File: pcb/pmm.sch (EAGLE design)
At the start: 20 parts, among them IC3 STM32F042F4, SW3 324_SW, SW4 324_SW, U2 USBC_16P, U4 XC6206_DEV

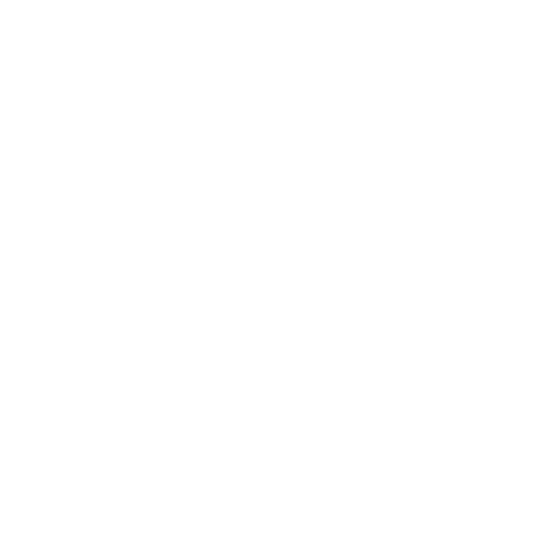
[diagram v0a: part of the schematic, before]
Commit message: hotshoe done
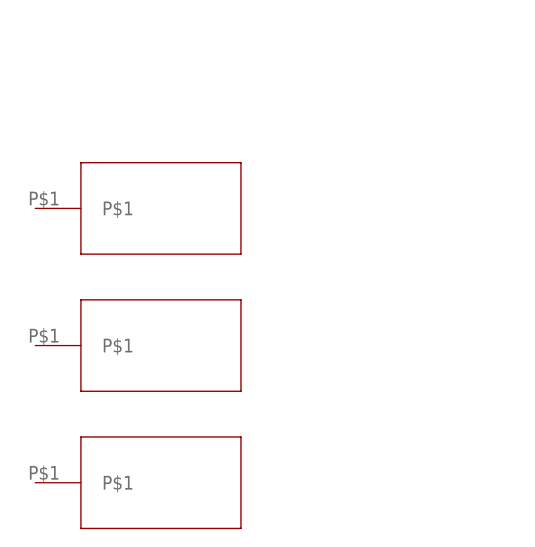
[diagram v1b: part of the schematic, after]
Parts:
- added U$3, U$4, U$5: POGO_1.5MM_HOLE, apricot:POGO_1.5MM_HOLE
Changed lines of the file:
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@@
 <layer number="117" name="secv21" color="7" fill="1" visible="yes" active="yes"/>
 <layer number="118" name="Rect_Pads" color="7" fill="1" visible="yes" active="yes"/>
+<layer number="119" name="PF_Ref" color="7" fill="1" visible="yes" active="yes"/>
 <layer number="120" name="120" color="7" fill="1" visible="yes" active="yes"/>
 <layer number="121" name="_tsilk" color="7" fill="1" visible="yes" active="yes"/>
@@
 <layer number="131" name="tAdjust" color="7" fill="1" visible="yes" active="yes"/>
 <layer number="132" name="bAdjust" color="7" fill="1" visible="yes" active="yes"/>
+<layer number="133" name="bottom_silk" color="7" fill="1" visible="yes" active="yes"/>
+<layer number="134" name="silk_top" color="7" fill="1" visible="yes" active="yes"/>
+<layer number="135" name="silk_bottom" color="7" fill="1" visible="yes" active="yes"/>
+<layer number="136" name="silktop" color="7" fill="1" visible="yes" active="yes"/>
+<layer number="137" name="silkbottom" color="7" fill="1" visible="yes" active="yes"/>
+<layer number="138" name="EEE" color="7" fill="1" visible="yes" active="yes"/>
+<layer number="139" name="_tKeepout" color="7" fill="1" visible="yes" active="yes"/>
+<layer number="140" name="mbKeepout" color="7" fill="1" visible="yes" active="yes"/>
+<layer number="141" name="ASSEMBLY_TOP" color="7" fill="1" visible="yes" active="yes"/>
+<layer number="142" name="mbRestrict" color="7" fill="1" visible="yes" active="yes"/>
+<layer number="143" name="PLACE_BOUND_TOP" color="7" fill="1" visible="yes" active="yes"/>
 <layer number="144" name="Drill_legend" color="7" fill="1" visible="yes" active="yes"/>
 <layer number="145" name="DrillLegend_01-02" color="7" fill="1" visible="yes" active="yes"/>
@@
 <layer number="154" name="FabDoc2" color="7" fill="1" visible="yes" active="yes"/>
 <layer number="155" name="FabDoc3" color="7" fill="1" visible="yes" active="yes"/>
+<layer number="166" name="AntennaArea" color="7" fill="1" visible="yes" active="yes"/>
+<layer number="168" name="4mmHeightArea" color="7" fill="1" visible="yes" active="yes"/>
+<layer number="191" name="mNets" color="7" fill="1" visible="yes" active="yes"/>
+<layer number="192" name="mBusses" color="7" fill="1" visible="yes" active="yes"/>
+<layer number="193" name="mPins" color="7" fill="1" visible="yes" active="yes"/>
+<layer number="194" name="mSymbols" color="7" fill="1" visible="yes" active="yes"/>
+<layer number="195" name="mNames" color="7" fill="1" visible="yes" active="yes"/>
+<layer number="196" name="mValues" color="7" fill="1" visible="yes" active="yes"/>
 <layer number="199" name="Contour" color="7" fill="1" visible="yes" active="yes"/>
 <layer number="200" name="200bmp" color="1" fill="10" visible="no" active="no"/>
@@
 <layer number="250" name="Descript" color="3" fill="1" visible="no" active="no"/>
 <layer number="251" name="SMDround" color="12" fill="11" visible="no" active="no"/>
+<layer number="253" name="Extra" color="7" fill="1" visible="yes" active="yes"/>
 <layer number="254" name="cooling" color="7" fill="1" visible="yes" active="yes"/>
 <layer number="255" name="routoute" color="7" fill="1" visible="yes" active="yes"/>
@@
 <part name="U$1" library="3pos_slide_switch_centered" deviceset="M2_SCREW_DEV" device=""/>
 <part name="U$2" library="3pos_slide_switch_centered" deviceset="M2_SCREW_DEV" device=""/>
+<part name="U$3" library="apricot" deviceset="POGO_1.5MM_HOLE" device=""/>
+<part name="U$4" library="apricot" deviceset="POGO_1.5MM_HOLE" device=""/>
+<part name="U$5" library="apricot" deviceset="POGO_1.5MM_HOLE" device=""/>
 </parts>
 <sheets>
@@
 <instance part="U$1" gate="G$1" x="-66.04" y="114.3" smashed="yes"/>
 <instance part="U$2" gate="G$1" x="-66.04" y="101.6" smashed="yes"/>
+<instance part="U$3" gate="G$1" x="-88.9" y="5.08" smashed="yes"/>
+<instance part="U$4" gate="G$1" x="-88.9" y="-10.16" smashed="yes"/>
+<instance part="U$5" gate="G$1" x="-88.9" y="-25.4" smashed="yes"/>
 </instances>
 <busses>

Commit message: working on PCB
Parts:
- added BT1: BU2032SM-G, BU2032SM-G:BU2032SM-G
- added C20, C21: 1uF, clock:CAP0805
- added C22, C23: 2.2uF, clock:CAP0805
- added J1: AUDIO_JACK_3.5MM_PTH, SparkFun-Connectors:AUDIO_JACK_3.5MM_PTH
- added J2: FFC3B07-05-T, FFC3B07-05-T:FFC3B07-05-T
- added R7: 390K, SparkFun-Passives:RESISTOR0805-RES
- added R8: 5.1K, joyAnalog:RESISTOR0805-RES
- added SW1: (no value), tx:SWITCH-SPDTTDFGDFG
- added U1: (no value), lul:LUL_DISP_OLED_UG-2864HSWEG01
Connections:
- new net N$12: U1.SDIN
- new net N$14: U1.SCLK
- new net N$16: U1.DC
- new net N$35: C20.2, U1.C2P
- new net N$36: C20.1, U1.C2N
- new net N$37: C21.2, U1.C1P
- new net N$38: C21.1, U1.C1N
- new net N$39: R7.2, U1.IREF
- new net N$40: C22.2, U1.VCOMH
- new net N$41: C23.2, U1.VCC
- new net N$43: R8.1, U1./RES
- net +3V3: now also U1.VBAT, U1.VDD
- net GND: now also C22.1, C23.1, R7.1, R8.2, U1.VSS
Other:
- moved on the sheet: C1, C2, R1, R2

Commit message: working on PCB
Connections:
- net N$16 renamed OLED_DC
- net N$3 renamed SWCLK
- net N$4 renamed SWDIO
- net N$43 renamed OLED_RESET
- net N$6 renamed UART2_TX
- removed net N$12: U1.SDIN
- removed net N$14: U1.SCLK
- new net OLED_CS: U1./CS
- new net OLED_MOSI: IC3.PA7, U1.SDIN
- new net OLED_SCK: IC3.PA5, U1.SCLK
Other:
- moved on the sheet: BT1, LED1, LED3, R3, R4
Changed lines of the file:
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@@
 <part name="R3" library="SparkFun-Passives" deviceset="RESISTOR" device="0805-RES" value="1K"/>
 <part name="+3V4" library="backplane" deviceset="+3V3" device=""/>
-<part name="+3V6" library="supply1" library_urn="urn:adsk.eagle:library:371" deviceset="+3V3" device=""/>
-<part name="GND3" library="backplane" deviceset="GND" device=""/>
 <part name="+3V3" library="supply1" library_urn="urn:adsk.eagle:library:371" deviceset="+3V3" device=""/>
 <part name="U$12" library="3pos_slide_switch_centered" deviceset="M2_SCREW_DEV" device=""/>
@@
 <instance part="SW3" gate="G$1" x="91.44" y="55.88" smashed="yes" rot="R90"/>
 <instance part="SW4" gate="G$1" x="91.44" y="2.54" smashed="yes" rot="MR270"/>
-<instance part="LED1" gate="G$1" x="-71.12" y="53.34" smashed="yes" rot="R90">
-<attribute name="NAME" x="-66.548" y="56.896" size="1.778" layer="95" rot="R180"/>
-<attribute name="VALUE" x="-66.548" y="59.055" size="1.778" layer="96" rot="R180"/>
-</instance>
-<instance part="R4" gate="G$1" x="-60.96" y="53.34" smashed="yes" rot="R180">
-<attribute name="NAME" x="-57.15" y="51.8414" size="1.778" layer="95" rot="R180"/>
-<attribute name="VALUE" x="-57.15" y="56.642" size="1.778" layer="96" rot="R180"/>
-</instance>
-<instance part="+3V9" gate="G$1" x="-73.66" y="55.88" smashed="yes" rot="MR0">
-<attribute name="VALUE" x="-71.12" y="50.8" size="1.778" layer="96" rot="MR90"/>
+<instance part="LED1" gate="G$1" x="-25.4" y="-45.72" smashed="yes" rot="R90">
+<attribute name="NAME" x="-20.828" y="-42.164" size="1.778" layer="95" rot="R180"/>
+<attribute name="VALUE" x="-20.828" y="-40.005" size="1.778" layer="96" rot="R180"/>
+</instance>
+<instance part="R4" gate="G$1" x="-15.24" y="-45.72" smashed="yes" rot="R180">
+<attribute name="NAME" x="-11.43" y="-47.2186" size="1.778" layer="95" rot="R180"/>
+<attribute name="VALUE" x="-11.43" y="-42.418" size="1.778" layer="96" rot="R180"/>
+</instance>
+<instance part="+3V9" gate="G$1" x="-27.94" y="-43.18" smashed="yes" rot="MR0">
+<attribute name="VALUE" x="-25.4" y="-48.26" size="1.778" layer="96" rot="MR90"/>
 </instance>
 <instance part="+3V16" gate="G$1" x="106.68" y="73.66" smashed="yes" rot="MR0">
@@
 <attribute name="VALUE" x="343.916" y="30.099" size="1.778" layer="96" rot="R180"/>
 </instance>
-<instance part="LED3" gate="G$1" x="-71.12" y="43.18" smashed="yes" rot="R90">
-<attribute name="NAME" x="-66.548" y="46.736" size="1.778" layer="95" rot="R180"/>
-<attribute name="VALUE" x="-66.548" y="48.895" size="1.778" layer="96" rot="R180"/>
-</instance>
-<instance part="R3" gate="G$1" x="-60.96" y="43.18" smashed="yes" rot="R180">
-<attribute name="NAME" x="-57.15" y="41.6814" size="1.778" layer="95" rot="R180"/>
-<attribute name="VALUE" x="-57.15" y="46.482" size="1.778" layer="96" rot="R180"/>
-</instance>
-<instance part="+3V4" gate="G$1" x="-73.66" y="45.72" smashed="yes" rot="MR0">
-<attribute name="VALUE" x="-71.12" y="40.64" size="1.778" layer="96" rot="MR90"/>
-</instance>
-<instance part="+3V6" gate="G$1" x="-27.94" y="66.04" smashed="yes" rot="MR0">
-<attribute name="VALUE" x="-25.4" y="60.96" size="1.778" layer="96" rot="MR90"/>
-</instance>
-<instance part="GND3" gate="1" x="-17.78" y="55.88" smashed="yes">
-<attribute name="VALUE" x="-20.32" y="53.34" size="1.778" layer="96"/>
+<instance part="LED3" gate="G$1" x="-25.4" y="-55.88" smashed="yes" rot="R90">
+<attribute name="NAME" x="-20.828" y="-52.324" size="1.778" layer="95" rot="R180"/>
+<attribute name="VALUE" x="-20.828" y="-50.165" size="1.778" layer="96" rot="R180"/>
+</instance>
+<instance part="R3" gate="G$1" x="-15.24" y="-55.88" smashed="yes" rot="R180">
+<attribute name="NAME" x="-11.43" y="-57.3786" size="1.778" layer="95" rot="R180"/>
+<attribute name="VALUE" x="-11.43" y="-52.578" size="1.778" layer="96" rot="R180"/>
+</instance>
+<instance part="+3V4" gate="G$1" x="-27.94" y="-53.34" smashed="yes" rot="MR0">
+<attribute name="VALUE" x="-25.4" y="-58.42" size="1.778" layer="96" rot="MR90"/>
 </instance>
 <instance part="+3V3" gate="G$1" x="276.86" y="88.9" smashed="yes" rot="MR0">
@@
 <attribute name="VALUE" x="96.52" y="119.38" size="1.778" layer="96"/>
 </instance>
-<instance part="BT1" gate="G$1" x="25.4" y="78.74" smashed="yes">
-<attribute name="NAME" x="19.038640625" y="82.553790625" size="2.543790625" layer="95"/>
-<attribute name="VALUE" x="19.03816875" y="72.38211875" size="2.543940625" layer="96"/>
+<instance part="BT1" gate="G$1" x="-43.18" y="-17.78" smashed="yes">
+<attribute name="NAME" x="-49.541359375" y="-13.966209375" size="2.543790625" layer="95"/>
+<attribute name="VALUE" x="-49.54183125" y="-24.13788125" size="2.543940625" layer="96"/>
 </instance>
 <instance part="J1" gate="G$1" x="50.8" y="-58.42" smashed="yes">
@@
 </segment>
 </net>
-<net name="N$3" class="0">
+<net name="SWCLK" class="0">
 <segment>
 <pinref part="IC3" gate="G$1" pin="PA14"/>
-<wire x1="-17.78" y1="12.7" x2="-35.56" y2="12.7" width="0.1524" layer="91"/>
-<wire x1="-35.56" y1="12.7" x2="-35.56" y2="58.42" width="0.1524" layer="91"/>
-</segment>
-</net>
-<net name="N$4" class="0">
+<wire x1="-17.78" y1="12.7" x2="-40.64" y2="12.7" width="0.1524" layer="91"/>
+<label x="-40.64" y="12.7" size="1.778" layer="95"/>
+</segment>
+</net>
+<net name="SWDIO" class="0">
 <segment>
 <pinref part="IC3" gate="G$1" pin="PA13"/>
-<wire x1="-17.78" y1="15.24" x2="-33.02" y2="15.24" width="0.1524" layer="91"/>
-<wire x1="-33.02" y1="15.24" x2="-33.02" y2="58.42" width="0.1524" layer="91"/>
-</segment>
-</net>
-<net name="N$6" class="0">
-<segment>
-<pinref part="IC3" gate="G$1" pin="PA2"/>
-<wire x1="-17.78" y1="35.56" x2="-30.48" y2="35.56" width="0.1524" layer="91"/>
-<wire x1="-30.48" y1="35.56" x2="-30.48" y2="58.42" width="0.1524" layer="91"/>
+<wire x1="-17.78" y1="15.24" x2="-40.64" y2="15.24" width="0.1524" layer="91"/>
+<label x="-40.64" y="15.24" size="1.778" layer="95"/>
 </segment>
 </net>
@@
 </segment>
 </net>
-<net name="N$43" class="0">
+<net name="OLED_RESET" class="0">
 <segment>
 <pinref part="U1" gate="G$1" pin="/RES"/>
 <pinref part="R8" gate="G$1" pin="1"/>
 <wire x1="38.1" y1="134.62" x2="99.06" y2="134.62" width="0.1524" layer="91"/>
-<wire x1="38.1" y1="134.62" x2="-114.3" y2="134.62" width="0.1524" layer="91"/>
+<wire x1="38.1" y1="134.62" x2="12.7" y2="134.62" width="0.1524" layer="91"/>
 <junction x="38.1" y="134.62"/>
-</segment>
-</net>
-<net name="N$12" class="0">
+<label x="12.7" y="134.62" size="1.778" layer="95"/>
+</segment>
+</net>
+<net name="UART2_TX" class="0">
+<segment>
+<pinref part="IC3" gate="G$1" pin="PA2"/>
+<wire x1="-17.78" y1="35.56" x2="-40.64" y2="35.56" width="0.1524" layer="91"/>
+<label x="-40.64" y="35.56" size="1.778" layer="95"/>
+</segment>
+</net>
+<net name="OLED_MOSI" class="0">
 <segment>
 <pinref part="U1" gate="G$1" pin="SDIN"/>
-<wire x1="38.1" y1="127" x2="-73.66" y2="127" width="0.1524" layer="91"/>
-</segment>
-</net>
-<net name="N$14" class="0">
+<wire x1="38.1" y1="127" x2="12.7" y2="127" width="0.1524" layer="91"/>
+<label x="12.7" y="127" size="1.778" layer="95"/>
+</segment>
+<segment>
+<pinref part="IC3" gate="G$1" pin="PA7"/>
+<wire x1="-17.78" y1="22.86" x2="-40.64" y2="22.86" width="0.1524" layer="91"/>
+<label x="-40.64" y="22.86" size="1.778" layer="95"/>
+</segment>
+</net>
+<net name="OLED_SCK" class="0">
 <segment>
 <pinref part="U1" gate="G$1" pin="SCLK"/>
-<wire x1="38.1" y1="129.54" x2="-78.74" y2="129.54" width="0.1524" layer="91"/>
-</segment>
-</net>
-<net name="N$16" class="0">
+<wire x1="38.1" y1="129.54" x2="12.7" y2="129.54" width="0.1524" layer="91"/>
+<label x="12.7" y="129.54" size="1.778" layer="95"/>
+</segment>
+<segment>
+<pinref part="IC3" gate="G$1" pin="PA5"/>
+<wire x1="-17.78" y1="27.94" x2="-40.64" y2="27.94" width="0.1524" layer="91"/>
+<label x="-40.64" y="27.94" size="1.778" layer="95"/>
+</segment>
+</net>
+<net name="OLED_DC" class="0">
 <segment>
 <pinref part="U1" gate="G$1" pin="DC"/>
-<wire x1="38.1" y1="132.08" x2="-83.82" y2="132.08" width="0.1524" layer="91"/>
-</segment>
-</net>
+<wire x1="38.1" y1="132.08" x2="12.7" y2="132.08" width="0.1524" layer="91"/>
+<label x="12.7" y="132.08" size="1.778" layer="95"/>
+</segment>
+</net>
+<net name="OLED_CS" class="0">
+<segment>
+<pinref part="U1" gate="G$1" pin="/CS"/>
+<wire x1="38.1" y1="137.16" x2="12.7" y2="137.16" width="0.1524" layer="91"/>
+<label x="12.7" y="137.16" size="1.778" layer="95"/>
+</segment>
+</net>

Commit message: working on PCB
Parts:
- added U$6: PINHD5, adafruit_changed:PINHD5
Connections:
- net GND: now also U$4.P$1, U$5.P$1, U$6.5
- net SWCLK: now also U$6.2
- net SWDIO: now also U$6.3
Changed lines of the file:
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@@
 <part name="SW1" library="tx" deviceset="SWITCH-SPDT" device="TDFGDFG"/>
 <part name="J2" library="FFC3B07-05-T" deviceset="FFC3B07-05-T" device=""/>
+<part name="GND2" library="supply1" deviceset="GND" device=""/>
+<part name="GND3" library="supply1" deviceset="GND" device=""/>
+<part name="GND4" library="supply1" deviceset="GND" device=""/>
+<part name="U$6" library="adafruit_changed" deviceset="PINHD5" device=""/>
 </parts>
 <sheets>
@@
 <attribute name="VALUE" x="-25.4" y="-58.42" size="1.778" layer="96" rot="MR90"/>
 </instance>
-<instance part="+3V3" gate="G$1" x="276.86" y="88.9" smashed="yes" rot="MR0">
-<attribute name="VALUE" x="279.4" y="83.82" size="1.778" layer="96" rot="MR90"/>
+<instance part="+3V3" gate="G$1" x="276.86" y="99.06" smashed="yes" rot="MR0">
+<attribute name="VALUE" x="279.4" y="93.98" size="1.778" layer="96" rot="MR90"/>
 </instance>
 <instance part="U$12" gate="G$1" x="-144.78" y="78.74" smashed="yes"/>
@@
 <attribute name="NAME" x="109.22" y="-29.718" size="1.778" layer="95"/>
 <attribute name="VALUE" x="109.22" y="-53.34" size="1.778" layer="96"/>
+</instance>
+<instance part="GND2" gate="1" x="-106.68" y="-12.7" smashed="yes" rot="MR0">
+<attribute name="VALUE" x="-104.14" y="-15.24" size="1.778" layer="96" rot="MR0"/>
+</instance>
+<instance part="GND3" gate="1" x="-106.68" y="-27.94" smashed="yes" rot="MR0">
+<attribute name="VALUE" x="-104.14" y="-30.48" size="1.778" layer="96" rot="MR0"/>
+</instance>
+<instance part="GND4" gate="1" x="-88.9" y="25.4" smashed="yes" rot="MR0">
+<attribute name="VALUE" x="-86.36" y="22.86" size="1.778" layer="96" rot="MR0"/>
+</instance>
+<instance part="U$6" gate="G$1" x="-81.28" y="30.48" smashed="yes">
+<attribute name="NAME" x="-87.63" y="41.275" size="1.778" layer="95"/>
+<attribute name="VALUE" x="-87.63" y="20.32" size="1.778" layer="96"/>
 </instance>
 </instances>
@@
 <pinref part="GND30" gate="1" pin="GND"/>
 </segment>
+<segment>
+<pinref part="GND2" gate="1" pin="GND"/>
+<pinref part="U$4" gate="G$1" pin="P$1"/>
+<wire x1="-106.68" y1="-10.16" x2="-101.6" y2="-10.16" width="0.1524" layer="91"/>
+</segment>
+<segment>
+<pinref part="GND3" gate="1" pin="GND"/>
+<pinref part="U$5" gate="G$1" pin="P$1"/>
+<wire x1="-106.68" y1="-25.4" x2="-101.6" y2="-25.4" width="0.1524" layer="91"/>
+</segment>
+<segment>
+<pinref part="GND4" gate="1" pin="GND"/>
+<wire x1="-88.9" y1="27.94" x2="-83.82" y2="27.94" width="0.1524" layer="91"/>
+<pinref part="U$6" gate="G$1" pin="5"/>
+</segment>
 </net>
 <net name="+3V3" class="0">
@@
 <pinref part="C4" gate="G$1" pin="2"/>
 <pinref part="+3V3" gate="G$1" pin="+3V3"/>
+<wire x1="276.86" y1="96.52" x2="276.86" y2="86.36" width="0.1524" layer="91"/>
 </segment>
 <segment>
@@
 <label x="-40.64" y="12.7" size="1.778" layer="95"/>
 </segment>
+<segment>
+<wire x1="-83.82" y1="35.56" x2="-106.68" y2="35.56" width="0.1524" layer="91"/>
+<label x="-106.68" y="35.56" size="1.778" layer="95"/>
+<pinref part="U$6" gate="G$1" pin="2"/>
+</segment>
 </net>
 <net name="SWDIO" class="0">
@@
 <label x="-40.64" y="15.24" size="1.778" layer="95"/>
 </segment>
-</net>
+<segment>
+<wire x1="-83.82" y1="33.02" x2="-106.68" y2="33.02" width="0.1524" layer="91"/>
+<label x="-106.68" y="33.02" size="1.778" layer="95"/>
+<pinref part="U$6" gate="G$1" pin="3"/>
+</segment>
+</net>

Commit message: working on PCB
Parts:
- removed LED2, LED3: (no value), adafruit:LEDCHIP-LED0805
- removed R3, R6: 1K, SparkFun-Passives:RESISTOR0805-RES
- removed SW1: (no value), tx:SWITCH-SPDTTDFGDFG
- added JP1: (no value), adafruit_changed:PINHD-1X3CB
- added U$7: PINHD1X4, adafruit_changed:PINHD1X4
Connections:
- removed net N$1: LED3.C, R3.2
- removed net N$29: LED2.C, R6.2
- new net LIGHT_SENSE: J2.3
- new net N$2: IC3.PB1, U$3.P$1, U$7.2, U$7.3
- new net N$3: BT1.+, JP1.2
- net +3V3: now also J2.2, J2.4, JP1.3; no longer LED2.A, LED3.A
- net GND: now also BT1.-, J2.1, J2.5, J2.SHIELD, U$7.1, U$7.4; no longer R6.1
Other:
- moved on the sheet: J2

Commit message: working on PCB
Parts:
- added JP2, JP3: (no value), pinhead:PINHD-1X2
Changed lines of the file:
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@@
 <part name="+3V7" library="supply1" library_urn="urn:adsk.eagle:library:371" deviceset="+3V3" device=""/>
 <part name="JP1" library="adafruit_changed" deviceset="PINHD-1X3" device="CB"/>
+<part name="JP2" library="pinhead" library_urn="urn:adsk.eagle:library:325" deviceset="PINHD-1X2" device="" package3d_urn="urn:adsk.eagle:package:22435/2"/>
+<part name="JP3" library="pinhead" library_urn="urn:adsk.eagle:library:325" deviceset="PINHD-1X2" device="" package3d_urn="urn:adsk.eagle:package:22435/2"/>
 </parts>
 <sheets>
@@
 <attribute name="NAME" x="-107.315" y="-64.77" size="1.778" layer="95" rot="R90"/>
 <attribute name="VALUE" x="-93.98" y="-64.77" size="1.778" layer="96" rot="R90"/>
+</instance>
+<instance part="JP2" gate="G$1" x="-53.34" y="-43.18" smashed="yes">
+<attribute name="NAME" x="-59.69" y="-37.465" size="1.778" layer="95"/>
+<attribute name="VALUE" x="-59.69" y="-48.26" size="1.778" layer="96"/>
+</instance>
+<instance part="JP3" gate="G$1" x="-35.56" y="-33.02" smashed="yes">
+<attribute name="NAME" x="-41.91" y="-27.305" size="1.778" layer="95"/>
+<attribute name="VALUE" x="-41.91" y="-38.1" size="1.778" layer="96"/>
 </instance>
 </instances>
@@
 will not be understood (or retained) with this version.
 </note>
+<note version="8.3" severity="warning">
+Since Version 8.3, EAGLE supports the association of 3D packages
+with devices in libraries, schematics, and board files. Those 3D
+packages will not be understood (or retained) with this version.
+</note>
 </compatibility>

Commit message: working on PCB
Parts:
- removed JP2, JP3: (no value), pinhead:PINHD-1X2
- added C3: 1uF, clock:CAP0805
- added R3, R6: 5.1K, joyAnalog:RESISTOR0805-RES
- added U$8, U$9: PINHD1X2, adafruit_changed:PINHD1X2
- C2: value 1uF -> 100nF
- C4: value 1uF -> 2.2uF
- R4: value 1K -> 5K1
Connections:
- new net N$1: BT1.+, JP1.1
- new net PC_SYNC: IC3.PA4, J1.TIP, R6.1, U$8.2
- new net USER_LED: IC3.PA3, LED1.A
- net +3V3: now also JP1.2, R3.1, R6.2, U$6.1; no longer JP1.3, LED1.A, U4.OUT
- net GND: now also C3.1, J1.SLEEVE, R4.1, U$8.1, U$9.2
- net LIGHT_SENSE: now also IC3.PF0/OSC_IN, U$9.1
- net N$2: now also R3.2
- net N$3: now also C3.2, JP1.3, U4.OUT; no longer BT1.+, JP1.2
- net OLED_CS: now also IC3.PF1/OSC_OUT
- net OLED_DC: now also IC3.PA1
- net OLED_RESET: now also IC3.PA0
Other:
- moved on the sheet: C2, J1, JP1, R4

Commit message: working on PCB
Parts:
- U$3, U$4, U$5: value POGO_1.5MM_HOLE -> POGO_TH001; device apricot:POGO_1.5MM_HOLE -> apricot:POGO_TH001
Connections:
- net N$1 renamed VBAT
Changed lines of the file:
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@@
 <part name="U$1" library="3pos_slide_switch_centered" deviceset="M2_SCREW_DEV" device=""/>
 <part name="U$2" library="3pos_slide_switch_centered" deviceset="M2_SCREW_DEV" device=""/>
-<part name="U$3" library="apricot" deviceset="POGO_1.5MM_HOLE" device=""/>
-<part name="U$4" library="apricot" deviceset="POGO_1.5MM_HOLE" device=""/>
-<part name="U$5" library="apricot" deviceset="POGO_1.5MM_HOLE" device=""/>
+<part name="U$3" library="apricot" deviceset="POGO_TH001" device=""/>
+<part name="U$4" library="apricot" deviceset="POGO_TH001" device=""/>
+<part name="U$5" library="apricot" deviceset="POGO_TH001" device=""/>
 <part name="U1" library="lul" deviceset="LUL_DISP_OLED_UG-2864HSWEG01" device=""/>
 <part name="GND26" library="supply1" library_urn="urn:adsk.eagle:library:371" deviceset="GND" device=""/>
@@
 </segment>
 </net>
-<net name="N$1" class="0">
+<net name="VBAT" class="0">
 <segment>
 <pinref part="BT1" gate="G$1" pin="+"/>
